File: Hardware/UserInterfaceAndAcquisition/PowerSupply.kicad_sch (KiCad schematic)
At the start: 2 parts, among them J8 USB_B_Micro

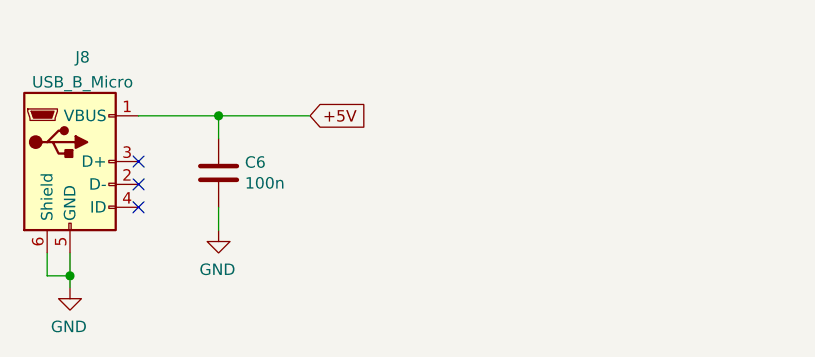
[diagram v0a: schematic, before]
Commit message: split PCB into separate designs
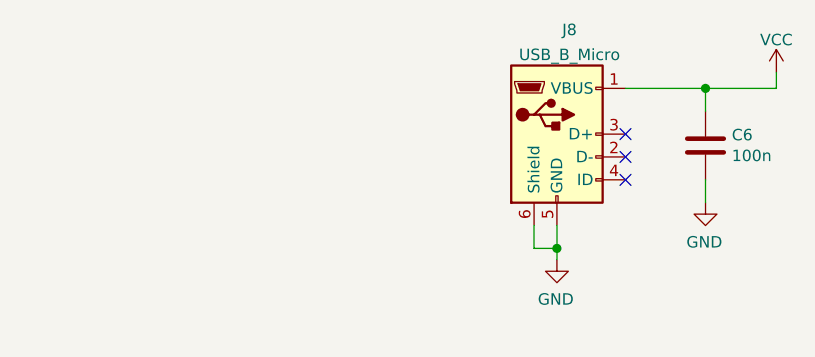
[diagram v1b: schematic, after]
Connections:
- net +5V renamed VCC
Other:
- moved on the sheet: C6, J8
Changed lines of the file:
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@@
 (kicad_sch (version 20210621) (generator eeschema)
   (paper "A4")
-  (junction (at 25.4 107.95) (diameter 1.016) (color 0 0 0 0))
-  (junction (at 41.91 90.17) (diameter 1.016) (color 0 0 0 0))
-  (no_connect (at 33.02 95.25))
-  (no_connect (at 33.02 97.79))
-  (no_connect (at 33.02 100.33))
-  (wire (pts (xy 22.86 105.41) (xy 22.86 107.95))
+  (junction (at 79.502 104.902) (diameter 1.016) (color 0 0 0 0))
+  (junction (at 96.012 87.122) (diameter 1.016) (color 0 0 0 0))
+  (no_connect (at 87.122 92.202))
+  (no_connect (at 87.122 94.742))
+  (no_connect (at 87.122 97.282))
+  (wire (pts (xy 76.962 102.362) (xy 76.962 104.902))
     (stroke (width 0) (type solid) (color 0 0 0 0))
   )
-  (wire (pts (xy 22.86 107.95) (xy 25.4 107.95))
+  (wire (pts (xy 76.962 104.902) (xy 79.502 104.902))
     (stroke (width 0) (type solid) (color 0 0 0 0))
   )
-  (wire (pts (xy 25.4 105.41) (xy 25.4 107.95))
+  (wire (pts (xy 79.502 102.362) (xy 79.502 104.902))
     (stroke (width 0) (type solid) (color 0 0 0 0))
   )
-  (wire (pts (xy 25.4 107.95) (xy 25.4 109.22))
+  (wire (pts (xy 79.502 104.902) (xy 79.502 106.172))
     (stroke (width 0) (type solid) (color 0 0 0 0))
   )
-  (wire (pts (xy 33.02 90.17) (xy 41.91 90.17))
+  (wire (pts (xy 87.122 87.122) (xy 96.012 87.122))
     (stroke (width 0) (type solid) (color 0 0 0 0))
   )
-  (wire (pts (xy 41.91 90.17) (xy 52.07 90.17))
+  (wire (pts (xy 96.012 87.122) (xy 103.886 87.122))
     (stroke (width 0) (type solid) (color 0 0 0 0))
   )
-  (wire (pts (xy 41.91 92.71) (xy 41.91 90.17))
+  (wire (pts (xy 96.012 89.662) (xy 96.012 87.122))
     (stroke (width 0) (type solid) (color 0 0 0 0))
   )
-  (wire (pts (xy 41.91 100.33) (xy 41.91 102.87))
+  (wire (pts (xy 96.012 97.282) (xy 96.012 99.822))
     (stroke (width 0) (type solid) (color 0 0 0 0))
   )
-  (global_label "+5V" (shape input) (at 52.07 90.17 0) (fields_autoplaced)
-    (effects (font (size 1.27 1.27)) (justify left))
-    (property "Intersheet References" "${INTERSHEET_REFS}" (id 0) (at 0 0 0)
+  (wire (pts (xy 103.886 85.344) (xy 103.886 87.122))
+    (stroke (width 0) (type solid) (color 0 0 0 0))
+  )
+  (symbol (lib_id "power:VCC") (at 103.886 85.344 0) (unit 1)
+    (in_bom yes) (on_board yes) (fields_autoplaced)
+    (property "Reference" "#PWR0101" (id 0) (at 103.886 89.154 0)
       (effects (font (size 1.27 1.27)) hide)
     )
-  )
-  (symbol (lib_id "power:GND") (at 25.4 109.22 0) (mirror y) (unit 1)
-    (in_bom yes) (on_board yes)
-    (property "Reference" "#PWR02" (id 0) (at 25.4 115.57 0)
+    (property "Value" "VCC" (id 1) (at 103.886 81.7394 0))
+    (property "Footprint" "" (id 2) (at 103.886 85.344 0)
       (effects (font (size 1.27 1.27)) hide)
     )
-    (property "Value" "GND" (id 1) (at 25.273 113.6142 0))
-    (property "Footprint" "" (id 2) (at 25.4 109.22 0)
-      (effects (font (size 1.27 1.27)) hide)
-    )
-    (property "Datasheet" "" (id 3) (at 25.4 109.22 0)
+    (property "Datasheet" "" (id 3) (at 103.886 85.344 0)
       (effects (font (size 1.27 1.27)) hide)
     )
     (pin "1")
   )
-  (symbol (lib_id "power:GND") (at 41.91 102.87 0) (mirror y) (unit 1)
+  (symbol (lib_id "power:GND") (at 79.502 106.172 0) (mirror y) (unit 1)
     (in_bom yes) (on_board yes)
-    (property "Reference" "#PWR028" (id 0) (at 41.91 109.22 0)
+    (property "Reference" "#PWR02" (id 0) (at 79.502 112.522 0)
       (effects (font (size 1.27 1.27)) hide)
     )
-    (property "Value" "GND" (id 1) (at 41.783 107.2642 0))
-    (property "Footprint" "" (id 2) (at 41.91 102.87 0)
+    (property "Value" "GND" (id 1) (at 79.375 110.5662 0))
+    (property "Footprint" "" (id 2) (at 79.502 106.172 0)
       (effects (font (size 1.27 1.27)) hide)
     )
-    (property "Datasheet" "" (id 3) (at 41.91 102.87 0)
+    (property "Datasheet" "" (id 3) (at 79.502 106.172 0)
       (effects (font (size 1.27 1.27)) hide)
     )
     (pin "1")
   )
-  (symbol (lib_id "Device:C") (at 41.91 96.52 0) (mirror y) (unit 1)
+  (symbol (lib_id "power:GND") (at 96.012 99.822 0) (mirror y) (unit 1)
     (in_bom yes) (on_board yes)
-    (property "Reference" "C6" (id 0) (at 44.831 95.3516 0)
+    (property "Reference" "#PWR028" (id 0) (at 96.012 106.172 0)
+      (effects (font (size 1.27 1.27)) hide)
+    )
+    (property "Value" "GND" (id 1) (at 95.885 104.2162 0))
+    (property "Footprint" "" (id 2) (at 96.012 99.822 0)
+      (effects (font (size 1.27 1.27)) hide)
+    )
+    (property "Datasheet" "" (id 3) (at 96.012 99.822 0)
+      (effects (font (size 1.27 1.27)) hide)
+    )
+    (pin "1")
+  )
+  (symbol (lib_id "Device:C") (at 96.012 93.472 0) (mirror y) (unit 1)
+    (in_bom yes) (on_board yes)
+    (property "Reference" "C6" (id 0) (at 98.933 92.3036 0)
       (effects (font (size 1.27 1.27)) (justify right))
     )
-    (property "Value" "100n" (id 1) (at 44.831 97.663 0)
+    (property "Value" "100n" (id 1) (at 98.933 94.615 0)
       (effects (font (size 1.27 1.27)) (justify right))
     )
-    (property "Footprint" "Capacitor_SMD:C_0805_2012Metric_Pad1.15x1.40mm_HandSolder" (id 2) (at 40.9448 100.33 0)
+    (property "Footprint" "Capacitor_SMD:C_0805_2012Metric_Pad1.15x1.40mm_HandSolder" (id 2) (at 95.0468 97.282 0)
       (effects (font (size 1.27 1.27)) hide)
     )
-    (property "Datasheet" "~" (id 3) (at 41.91 96.52 0)
+    (property "Datasheet" "~" (id 3) (at 96.012 93.472 0)
       (effects (font (size 1.27 1.27)) hide)
     )
@@
     (pin "2")
   )
-  (symbol (lib_id "Connector:USB_B_Micro") (at 25.4 95.25 0) (unit 1)
+  (symbol (lib_id "Connector:USB_B_Micro") (at 79.502 92.202 0) (unit 1)
     (in_bom yes) (on_board yes) (fields_autoplaced)
-    (property "Reference" "J8" (id 0) (at 26.797 83.6634 0))
-    (property "Value" "USB_B_Micro" (id 1) (at 26.797 86.4385 0))
-    (property "Footprint" "Connector_USB:USB_Micro-B_Molex-105017-0001" (id 2) (at 29.21 96.52 0)
+    (property "Reference" "J8" (id 0) (at 80.899 80.6154 0))
+    (property "Value" "USB_B_Micro" (id 1) (at 80.899 83.3905 0))
+    (property "Footprint" "Connector_USB:USB_Micro-B_Molex-105017-0001" (id 2) (at 83.312 93.472 0)
       (effects (font (size 1.27 1.27)) hide)
     )
-    (property "Datasheet" "~" (id 3) (at 29.21 96.52 0)
+    (property "Datasheet" "~" (id 3) (at 83.312 93.472 0)
       (effects (font (size 1.27 1.27)) hide)
     )
